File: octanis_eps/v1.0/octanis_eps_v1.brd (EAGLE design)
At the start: 80 x 50 mm, 155 parts, among them IC1 OPA2333DGK, Q1 32.768kHz, Q100 BSS123, Q2 BSC0901NS, U1 CSD16327Q3_DQG_8, U10 CSD16327Q3_DQG_8, U11 CSD16327Q3_DQG_8, U12 TPS630250YFFT, U15 MSP430FR5969, U2 CSD16327Q3_DQG_8, U3 CSD16327Q3_DQG_8, U5 TPS2022D, U6 TPS630250YFFT, U7 TPS630250YFFT, U8 TPS61232, U9 BQ24650_RVA_16

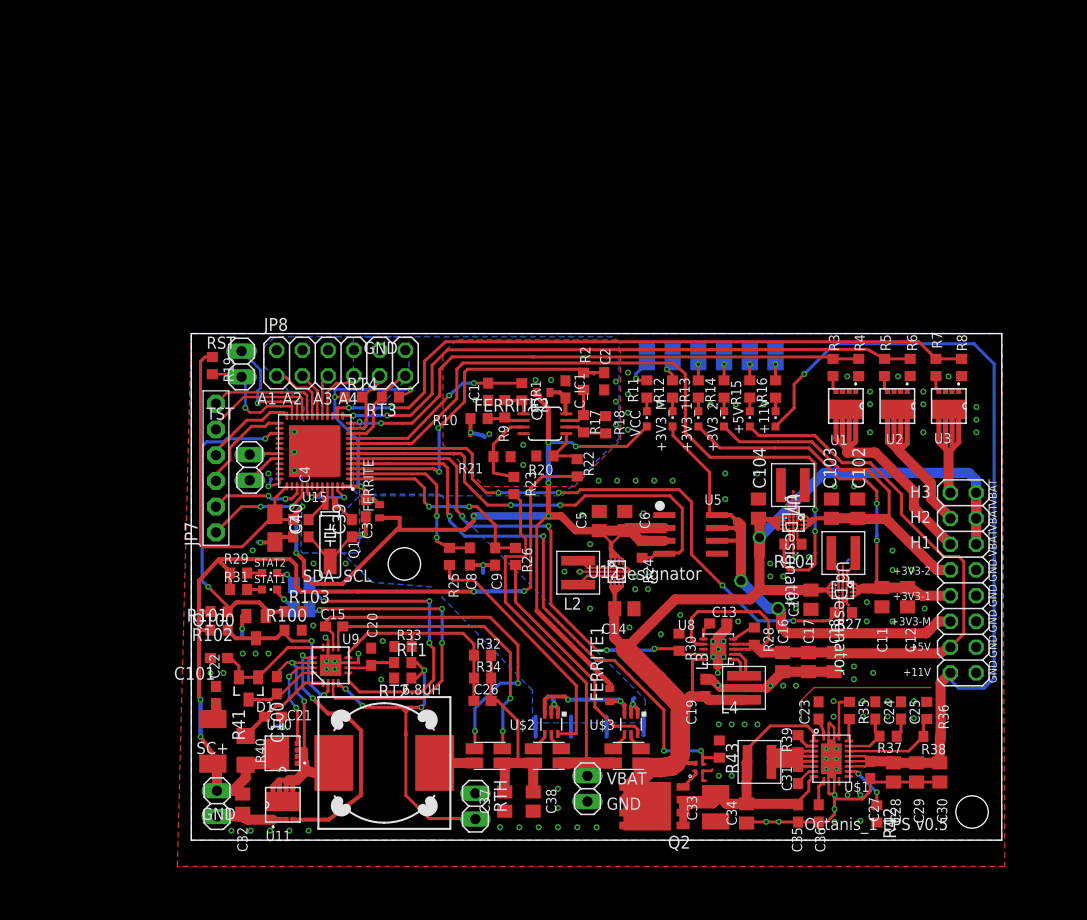
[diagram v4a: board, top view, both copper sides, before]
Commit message: removed ground loops
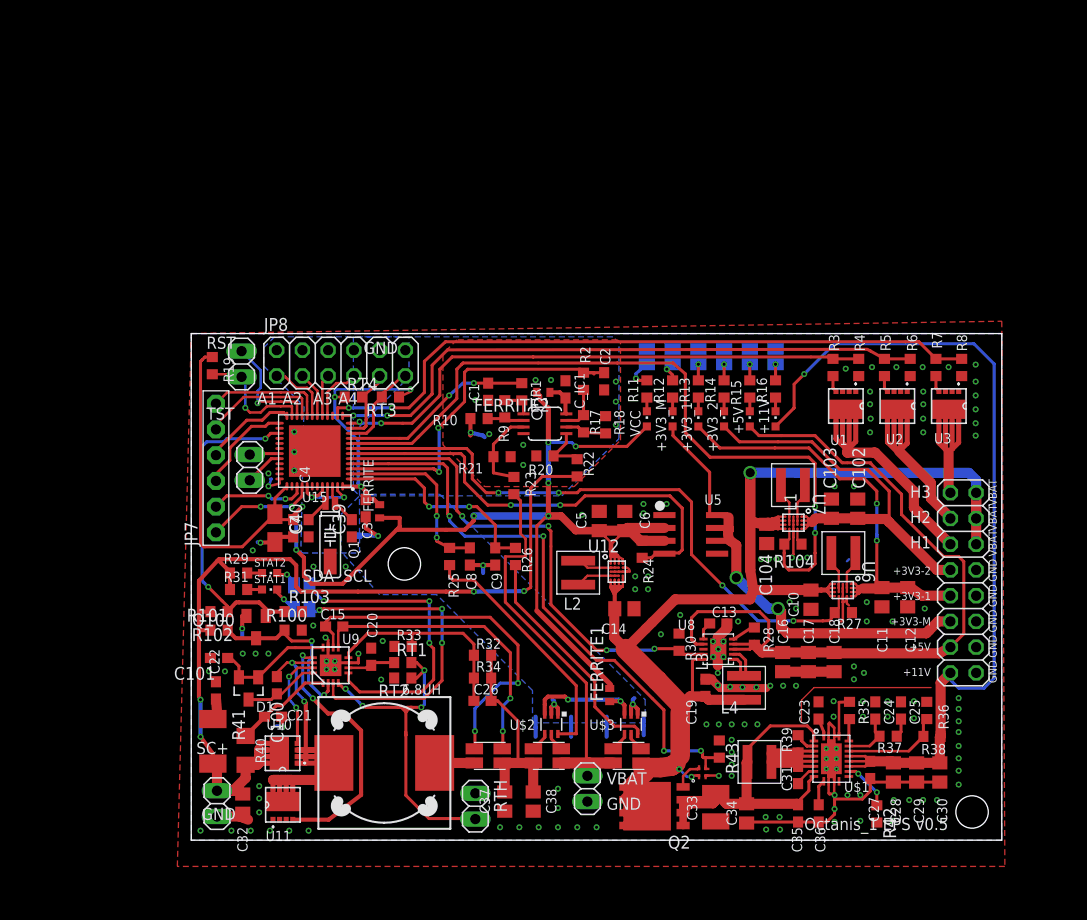
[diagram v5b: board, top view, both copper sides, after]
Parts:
- removed U$4: MIC4414, Octanis1_EPS:QFN-4
- added U$5: MIC5019, Octanis1_EPS:QFN-4
- moved C104 2.62 mm to (56.8, 30.2), turned to 270 degrees
- moved C22 0.46 mm to (2.44, 14.8)
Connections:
- net AGND: no longer C39.1, C40.1, Q1.P3
- net BAT_OUT: now also U$5.P$1, U$5.P1; no longer U$4.P$4, U$4.P4
- net EN_12V: now also U$5.P$3, U$5.P3; no longer U$4.P$3, U$4.P3
- net GND: now also C39.1, C40.1, Q1.P3, U$5.P$2, U$5.P2; no longer U$4.P$2, U$4.P2
- net N$10: now also U$5.P$4, U$5.P4; no longer U$4.P$1, U$4.P1
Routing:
- net N$76: track 29.8 -> 48.1 mm
- net GND: track 122.7 -> 106.9 mm, vias 123 -> 134
- net BAT_OUT: track 131.9 -> 146.9 mm, vias 1 -> 3
- net AGND: track 36.5 -> 30.6 mm
- net SC+: track 88.6 -> 92.3 mm
- net +3V3_M: track 49.7 -> 46.9 mm
- net +3V3_2: track 43.5 -> 42.5 mm
- net N$10: track 2.16 -> 2.99 mm

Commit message: reworked silkscreen
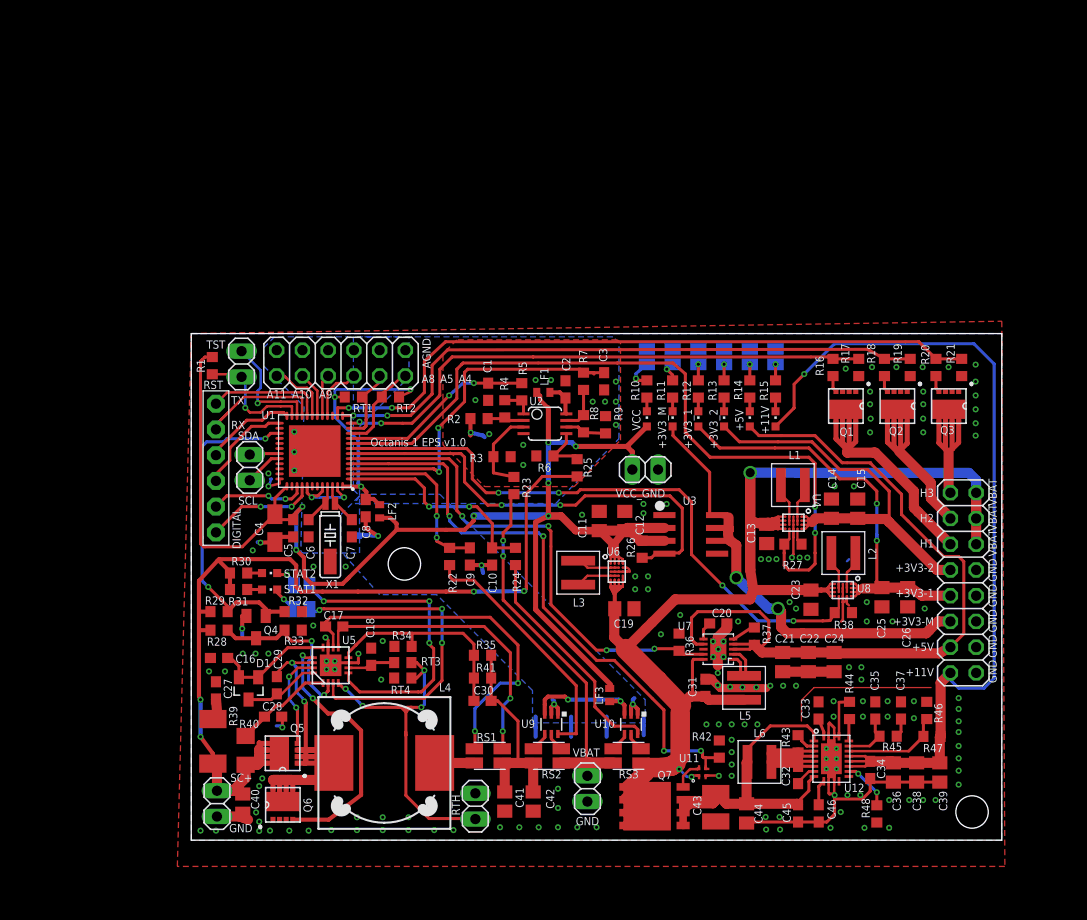
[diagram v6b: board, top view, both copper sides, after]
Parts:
- removed 6.8UH: DR127, inductors:DR127
- removed C100, C_IC1: 100nF, rcl:C0603
- removed C101: 1uF, rcl:C0603
- removed C102, C103: 22uF, resistor:C0805
- removed C104: 10uF, resistor:C0805
- removed IC1: OPA2333DGK, linear:MSOP08
- removed JP8: (no value), Headerlibrary:2X06
- removed L100: 1uH, Coilcraft:XFL4020
- removed R100, R101: (no value), rcl:R0603
- removed R102, R103: 1M, rcl:R0603
- removed R104: 1M, resistor:R0603
- removed U$1: TPS61088, texasinstruments:R-PVQFN-N20
- removed U$2, U$3: INA213, Octanis1_EPS:SC70-6
- removed U$5: MIC5019, Octanis1_EPS:QFN-4
- removed U15: MSP430FR5969, chips:S-PVQFN-N48
- added C41, C42, C44: 10uF, resistor:C0805
- added C43: 47uF Tantal, rcl:C1210
- added C45: 100nF, rcl:C0603
- added C46: 47nF, rcl:C0603
- added JP1, VCC_GND: (no value), Headerlibrary:1X02
- added L5: 1uH, Coilcraft:XFL4020
- added L6: 1.5uH, Coilcraft:XFL4020
- added Q3, Q5, Q6: CSD16327Q3_DQG_8, texasinstruments:DQG8
- added Q7: BSC0901NS, transistor-power:PG-TDSON-8
- added R44: 100k, resistor:R0603
- added R45: 150-220k, resistor:R0603
- added R46: 56k, resistor:R0603
- added R47: 470k, resistor:R0603
- added R48: dnp, resistor:R0603
- added U4: TPS630250YFFT, texasinstruments:YFF0020AEBA
- added X1: 32.768kHz, microcrystal:MS3V-T1R
- C10: value 10uF -> 1.5uF; device resistor:C0805 -> rcl:C0603
- C13: value 10nF -> 10uF; device rcl:C0603 -> resistor:C0805
- C14, C38: value 10uF -> 22uF
- C15: value 100nF -> 22uF; device rcl:C0603 -> resistor:C0805
- C16, C18: value 22uF -> 1uF; device resistor:C0805 -> rcl:C0603
- C17, C29, C5: value 22uF -> 100nF; device resistor:C0805 -> rcl:C0603
- C19: value 22uF -> 10uF; device rcl:C0603 -> resistor:C0805
- C2, C8: value 1.5uF -> 100nF
- C20: value 1uF -> 10nF
- C21: value 1u -> 22uF; device rcl:C0603 -> resistor:C0805
- C22: value 2.2uF -> 22uF; device rcl:C0603 -> resistor:C0805
- C23: value 2.2uF -> 10uF; device rcl:C0603 -> resistor:C0805
- C24: value 150pF -> 22uF; device rcl:C0603 -> resistor:C0805
- C25: value 4.7nF -> 22uF; device rcl:C0603 -> resistor:C0805
- C26: value 22pF -> 22uF; device rcl:C0603 -> resistor:C0805
- C27: value 1uF -> 2.2uF
- C28: value 22uF -> 1u; device resistor:C0805 -> rcl:C0603
- C3: value 100nF -> 1.5uF
- C30: value 22uF -> 22pF; device resistor:C0805 -> rcl:C0603
- C31: value 100nF -> 22uF
- C32: value 10uF -> 100nF; device resistor:C0805 -> rcl:C0603
- C33: value 47uF Tantal -> 2.2uF; device rcl:C1210 -> rcl:C0603
- C34: value 10uF -> 1uF; device resistor:C0805 -> rcl:C0603
- C35: value 100nF -> 150pF
- C36: value 47nF -> 22uF; device rcl:C0603 -> resistor:C0805
- C37: value 10uF -> 4.7nF; device resistor:C0805 -> rcl:C0603
- C39: value 12pF -> 22uF; device rcl:C0603 -> resistor:C0805
- C4: value 100nF -> 10uF; device rcl:C0603 -> rcl:A/3216-18R
- C40: value 12pF -> 10uF; device rcl:C0603 -> resistor:C0805
- C6: value 22uF -> 12pF; device resistor:C0805 -> rcl:C0603
- C7: value 10uF -> 12pF; device rcl:A/3216-18R -> rcl:C0603
- JP2: device Headerlibrary:1X02 -> Headerlibrary:2X06
- L4: value 1.5uH -> DR127_6u8; device Coilcraft:XFL4020 -> inductors:DR127
- Q1: value 32.768kHz -> CSD16327Q3_DQG_8; device microcrystal:MS3V-T1R -> texasinstruments:DQG8
- Q2: value BSC0901NS -> CSD16327Q3_DQG_8; device transistor-power:PG-TDSON-8 -> texasinstruments:DQG8
- R1: value 1k -> 10k
- R10, R18, R22: value 200k -> 1k
- R14: value 1k -> 1.5k
- R15: value 1.5k -> 4.7k
- R16: value 4.7k -> 1k
- R17, R21, R32: value 100k -> 1M
- R19: value 10k -> 1M
- R2, R25: value 1k -> 200k
- R20: value 100k -> 1k
- R24: value 1M -> 1k; device resistor:R0603 -> rcl:R0603
- R26: value 1k -> 1M; device rcl:R0603 -> resistor:R0603
- R29: value 4k7 -> (none)
- R3: value 1k -> 100k
- R30: value 1M -> 4k7
- R33: value 100k -> (none)
- R34: value 2.2M -> 100k
- R35: device resistor:R0603 -> rcl:R0603
- R36: value 56k -> 1M; device resistor:R0603 -> rcl:R0603
- R37: value 150-220k -> 1M; device resistor:R0603 -> rcl:R0603
- R38: value 470k -> 1M
- R39: value 47k -> 2; device resistor:R0603 -> rcl:R2010
- R4, R6, R8: value 1M -> 100k
- R41: value 2 -> 2.2M; device rcl:R2010 -> rcl:R0603
- R42: value dnp -> 1M; device resistor:R0603 -> rcl:R0603
- R43: value 1M -> 47k; device rcl:R0603 -> resistor:R0603
- R9: value 100k -> 200k
- RS1: value RSENSE1 10mOhm -> 10m
- RS2: value RSENSE2 -> 50m
- RS3: value RSENSE1 -> 50m
- RT2: value 8501 -> 2723
- RT4: value 2723 -> 8501
- U1: value CSD16327Q3_DQG_8 -> MSP430FR5969; device texasinstruments:DQG8 -> chips:S-PVQFN-N48
- U10: value CSD16327Q3_DQG_8 -> INA213; device texasinstruments:DQG8 -> Octanis1_EPS:SC70-6
- U11: value CSD16327Q3_DQG_8 -> MIC5019; device texasinstruments:DQG8 -> Octanis1_EPS:QFN-4
- U12: value TPS630250YFFT -> TPS61088; device texasinstruments:YFF0020AEBA -> texasinstruments:R-PVQFN-N20
- U2: value CSD16327Q3_DQG_8 -> OPA2333DGK; device texasinstruments:DQG8 -> linear:MSOP08
- U3: value CSD16327Q3_DQG_8 -> TPS2022D; device texasinstruments:DQG8 -> Octanis1_EPS:SO8
- U5: value TPS2022D -> BQ24650_RVA_16; device Octanis1_EPS:SO8 -> octanis_eps_v05:RVA16_2P14X2P14
- U7: value TPS630250YFFT -> TPS61232; device texasinstruments:YFF0020AEBA -> texasinstruments:S-PVSON-N10
- U8: value TPS61232 -> TPS630250YFFT; device texasinstruments:S-PVSON-N10 -> texasinstruments:YFF0020AEBA
- U9: value BQ24650_RVA_16 -> INA213; device octanis_eps_v05:RVA16_2P14X2P14 -> Octanis1_EPS:SC70-6
- moved R19 68.9 mm to (71.0, 46.7), turned to 270 degrees
- moved C27 65.1 mm to (2.44, 14.8)
- moved C29 63.7 mm to (8.45, 15.3), turned to 270 degrees
- moved C39 62.8 mm to (73.9, 6.68)
- moved C28 61.5 mm to (8.08, 12.2), turned to 0 degrees
- moved C22 58.5 mm to (60.9, 17.6), turned to 270 degrees
- moved R39 57.8 mm to (2.13, 9.75)
- moved C16 55.6 mm to (2.74, 18.0), turned to 180 degrees
- moved C32 54.9 mm to (59.9, 6.43), turned to 270 degrees
- moved C15 53.0 mm to (65.8, 32.7), turned to 90 degrees
- moved R28 52.9 mm to (2.74, 22.6), turned to 180 degrees
- moved Q1 52.8 mm to (64.6, 42.8), turned to 270 degrees
- moved U1 52.6 mm to (12.2, 38.4), turned to 180 degrees
- moved C21 50.6 mm to (58.4, 17.6), turned to 270 degrees
- moved C17 46.9 mm to (14.1, 21.1), turned to 180 degrees
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- renumbered FERRITE to LF2, FERRITE1 to LF3, FERRITE2 to LF1, J1 to J107, J2 to J106, J3 to J105, J4 to J104, J5 to J103, J6 to J102, J7 to J101, J8 to J100, JP7 to DIGITAL, Q100 to Q4, RSENSE1 to RS2, R_SENSE1 to RS1, R_SENSE2 to RS3
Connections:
- net +12V: now also C34.2, C36.2, C38.2, C39.2, R47.2, U12.P$14, U12.P$15, U12.P$16; no longer C27.2, C28.2, C29.2, C30.2, R38.2, U$1.P$14, U$1.P$15, U$1.P$16
- net +3V3: now also C11.1, C12.1, C4.+, R1.2, R26.2, U1.37, U3.2, U3.3, U6.1, U6.2, U6.3, U6.4, VCC_GND.1; no longer C4.1, C6.1, C7.+, R19.2, R24.2, U12.1, U12.2, U12.3, U12.4, U15.37, U5.2, U5.3
- net +3V3_1: now also C25.1, C26.1, U8.1, U8.2, U8.3, U8.4; no longer C11.1, C12.1, U6.1, U6.2, U6.3, U6.4
- net +3V3_2: now also C14.1, C15.1, U4.1, U4.2, U4.3, U4.4; no longer C102.1, C103.1, U7.1, U7.2, U7.3, U7.4
- net +3V3_M: now also U3.6, U3.7, U3.8; no longer U5.6, U5.7, U5.8
- net +5V: now also C21.1, C22.1, C24.1, R37.2, U7.3, U7.4, U7.7; no longer C16.1, C17.1, C18.1, R28.2, U8.3, U8.4, U8.7
- net A4_EXT: now also JP2.11, RT2.2, U1.10; no longer JP8.11, RT3.2, U15.10
- net A5_EXT: now also JP2.9, RT1.2, U1.11; no longer JP8.9, RT4.2, U15.11
- net AGND: now also C10.1, C3.1, C8.2, JP2.10, JP2.12, JP2.2, JP2.4, JP2.6, JP2.8, R2.2, R3.1, R6.1, R9.2, U1.41, U1.44, U1.47, U10.1, U10.2, U2.4, U9.1, U9.2; no longer C3.2, C8.1, C_IC1.1, IC1.4, JP8.10, JP8.12, JP8.2, JP8.4, JP8.6, JP8.8, R10.2, R18.2, R20.1, R21.1, U$2.1, U$2.2, U$3.1, U$3.2, U15.41, U15.44, U15.47
- net AVCC: now also C8.1, RT1.1, RT2.1, U1.48; no longer C3.1, RT3.1, RT4.1, U15.48
- net AVCC1: now also U10.3, U9.3; no longer U$2.3, U$3.3
- net AVCC2: now also C2.2, U2.8; no longer C_IC1.2, IC1.8
- net A_EXT1: now also JP2.7, U1.16; no longer JP8.7, U15.16
- net A_EXT2: now also JP2.5, U1.17; no longer JP8.5, U15.17
- net A_EXT3: now also JP2.3, U1.18; no longer JP8.3, U15.18
- net A_EXT4: now also JP2.1, U1.19; no longer JP8.1, U15.19
- net BAT_11V: now also C43.1, C44.1, C45.1, L6.P$1, Q7.1, Q7.2, Q7.3, U12.P$2, U12.P$9; no longer C33.1, C34.1, C35.1, L4.P$1, Q2.1, Q2.2, Q2.3, U$1.P$2, U$1.P$9
- net BAT_OUT: now also C13.1, C23.1, C31.1, L5.P$1, Q7.5, Q7.6, Q7.7, Q7.8, U11.P$1, U11.P1, U4.17, U4.18, U4.19, U4.20, U6.16, U7.10, U8.17, U8.18, U8.19, U8.20; no longer C10.1, C104.1, C14.1, L3.P$1, Q2.5, Q2.6, Q2.7, Q2.8, U$5.P$1, U$5.P1, U12.16, U12.17, U12.18, U12.19, U12.20, U7.17, U7.18, U7.19, U7.20, U8.10
- net EN_12V: now also R42.2, U1.4, U11.P$3, U11.P3; no longer R43.2, U$5.P$3, U$5.P3, U15.4
- net EN_3V3_1: now also R38.1, U1.7, U8.16; no longer R27.1, U15.7, U6.16
- net EN_3V3_2: now also R27.1, U1.8, U4.16; no longer R104.1, U15.8, U7.16
- net EN_3V3_M: now also R26.1, U1.6, U3.4; no longer R24.1, U15.6, U5.4
- net EN_5V: now also R36.2, U1.5, U7.9; no longer R30.2, U15.5, U8.9
- net EN_HEAT1: now also R16.2, R17.1, U1.12; no longer R3.2, R4.1, U15.12
- net EN_HEAT2: now also R18.2, R19.1, U1.13; no longer R5.2, R6.1, U15.13
- net EN_HEAT3: now also R20.2, R21.1, U1.14; no longer R7.2, R8.1, U15.14
- net EN_SC: now also R28.1, R32.2, U1.27; no longer R102.1, R103.2, U15.27
- net GND: now also C15.2, C26.2, C27.2, C28.2, C31.2, C34.1, C36.1, C38.1, C4.-, C41.2, C42.2, C43.2, C44.2, C45.2, C46.2, C6.1, C7.1, Q1.1, Q1.2, Q1.3, Q2.1, Q2.2, Q2.3, Q3.1, Q3.2, Q3.3, Q6.1, Q6.2, Q6.3, R17.2, R19.2, R21.2, R32.1, R34.1, R38.2, R42.1, R44.1, R46.1, R48.2, RT4.2, U1.36, U1.VSS_QFN, U11.P$2, U11.P2, U12.P$20, U12.PGND1, U12.PGND10, U12.PGND11, U12.PGND12, U12.PGND2, U12.PGND3, U12.PGND4, U12.PGND5, U12.PGND6, U12.PGND7, U12.PGND8, U12.PGND9, U4.10, U4.11, U4.12, U4.8, U4.9, U5.11, U5.17, U5.7, U5.V, U5.V_1, U5.V_2, U5.V_3, U7.EXPAD, U7.GND1, U7.GND2, U7.GND3, U7.GND4, U7.GND5, U8.10, U8.11, U8.12, U8.8, U8.9, VCC_GND.2, X1.P3; no longer C10.2, C101.2, C102.2, C103.2, C104.2, C17.2, C27.1, C28.1, C29.1, C30.1, C32.1, C34.2, C36.2, C38.2, C4.2, C6.2, C7.-, Q1.P3, R100.1, R103.1, R104.2, R30.1, R35.1, R4.2, R42.2, R43.1, R6.2, R8.2, RT2.2, U$1.P$20, U$1.PGND1, U$1.PGND10, U$1.PGND11, U$1.PGND12, U$1.PGND2, U$1.PGND3, U$1.PGND4, U$1.PGND5, U$1.PGND6, U$1.PGND7, U$1.PGND8, U$1.PGND9, U$5.P$2, U$5.P2, U1.1, U1.2, U1.3, U11.1, U11.2, U11.3, U12.10, U12.11, U12.12, U12.8, U12.9, U15.36, U15.VSS_QFN, U2.1, U2.2, U2.3, U3.2, U3.3, U5.1, U7.10, U7.11, U7.12, U7.8, U7.9, U8.EXPAD, U8.GND1, U8.GND2, U8.GND3, U8.GND4, U8.GND5, U9.11, U9.17, U9.7, U9.V, U9.V_1, U9.V_2, U9.V_3
- net HEAT1: now also Q1.5, Q1.6, Q1.7, Q1.8; no longer U1.5, U1.6, U1.7, U1.8
- net HEAT2: now also Q2.5, Q2.6, Q2.7, Q2.8; no longer U2.5, U2.6, U2.7, U2.8
- net HEAT3: now also Q3.5, Q3.6, Q3.7, Q3.8; no longer U3.5, U3.6, U3.7, U3.8
- net I2C_SCL: now also U1.32; no longer U15.32
- net I2C_SDA: now also U1.31; no longer U15.31
- net IND: now also L5.P$2, U7.1, U7.2; no longer L3.P$2, U8.1, U8.2
- net I_IN: now also C9.2, R22.1, U1.2; no longer C8.2, R25.1, U15.2
- net I_OUT: now also C10.2, R24.1, U1.1; no longer C9.2, R26.1, U15.1
- net LED5: now also R14.2; no longer R15.2
- net N$1: now also L3.P$1, U6.13, U6.14, U6.15; no longer L2.P$1, U12.13, U12.14, U12.15
- net N$10: now also Q7.4, U11.P$4, U11.P4; no longer Q2.4, U$5.P$4, U$5.P4
- net N$11: now also L1.P$1, U4.13, U4.14, U4.15; no longer L100.P$1, U7.13, U7.14, U7.15
- net N$12: now also L1.P$2, U4.5, U4.6, U4.7; no longer L100.P$2, U7.5, U7.6, U7.7
- net N$13: now also JP1.1, R1.1, U1.23; no longer JP2.1, R19.1, U15.23
- net N$14: now also R14.1; no longer R15.1
- net N$15: now also JP1.2, U1.22; no longer JP2.2, U15.22
- net N$16: now also C7.2, U1.46, X1.P1; no longer C39.2, Q1.P1, U15.46
- net N$17: now also C6.2, U1.45, X1.P2; no longer C40.2, Q1.P2, U15.45
- net N$18: now also U1.25; no longer U15.25
- net N$19: now also R4.1, R5.2, U2.1; no longer IC1.1, R1.2, R9.1
- net N$2: now also R37.1, U7.5; no longer R28.1, U8.5
- net N$20: now also R2.1, R4.2, U2.2; no longer IC1.2, R10.1, R9.2
- net N$21: now also R3.2, U2.3; no longer IC1.3, R21.2
- net N$22: now also R7.2, R8.1, U2.7; no longer IC1.7, R17.1, R2.2
- net N$23: now also R8.2, R9.1, U2.6; no longer IC1.6, R17.2, R18.1
- net N$24: now also R25.1, R6.2, U2.5; no longer IC1.5, R20.2, R22.1
- net N$25: now also R24.2, U10.6; no longer R26.2, U$3.6
- net N$26: now also R22.2, U9.6; no longer R25.2, U$2.6
- net N$27: now also Q3.4, R20.1; no longer R7.1, U3.4
- net N$28: now also U1.24; no longer U15.24
- net N$29: now also U1.39; no longer U15.39
- net N$3: now also L3.P$2, U6.5, U6.6, U6.7; no longer L2.P$2, U12.5, U12.6, U12.7
- net N$30: now also U1.40; no longer U15.40
- net N$31: now also Q2.4, R18.1; no longer R5.1, U2.4
- net N$32: now also U10.4; no longer U$3.4
- net N$33: now also U10.5; no longer U$3.5
- net N$34: now also U9.4; no longer U$2.4
- net N$35: now also U9.5; no longer U$2.5
- net N$36: now also U1.21; no longer U15.21
- net N$37: now also Q1.4, R16.1; no longer R3.1, U1.4
- net N$38: now also C32.2, U12.P$8; no longer C31.2, U$1.P$8
- net N$39: now also R11.2; no longer R12.2
- net N$4: now also L4.2; no longer 6.8UH.2
- net N$40: now also R11.1; no longer R12.1
- net N$41: now also U1.20; no longer U15.20
- net N$42: now also C27.1, R39.1; no longer C22.1, R41.1
- net N$43: now also R10.2; no longer R11.2
- net N$45: now also R10.1; no longer R11.1
- net N$46: now also R13.2; no longer R14.2
- net N$47: now also R13.1; no longer R14.1
- net N$48: now also R15.2; no longer R16.2
- net N$49: now also R15.1; no longer R16.1
- net N$5: now also C20.1, U7.6; no longer C13.1, U8.6
- net N$50: now also C32.1, L6.P$2, R43.2, U12.P$4, U12.P$5, U12.P$6, U12.P$7; no longer C31.1, L4.P$2, R39.2, U$1.P$4, U$1.P$5, U$1.P$6, U$1.P$7
- net N$51: now also R12.2; no longer R13.2
- net N$52: now also R12.1; no longer R13.1
- net N$53: now also R43.1, U12.P$3; no longer R39.1, U$1.P$3
- net N$54: now also C37.1, R45.1; no longer C25.1, R37.1
- net N$56: now also C46.1, U12.P$10; no longer C36.1, U$1.P$10
- net N$57: now also R44.2, U12.P$19; no longer R35.2, U$1.P$19
- net N$58: now also C35.1, R45.2, U12.P$18; no longer C24.1, R37.2, U$1.P$18
- net N$59: now also C33.1, U12.P$1; no longer C23.1, U$1.P$1
- net N$6: now also L2.P$1, U8.13, U8.14, U8.15; no longer L1.P$1, U6.13, U6.14, U6.15
- net N$60: now also R46.2, R47.1, U12.P$17; no longer R36.2, R38.1, U$1.P$17
- net N$64: now also R29.1, R33.2, U5.2; no longer R100.2, R101.1, U9.2
- net N$69: now also R30.1; no longer R29.1
- net N$7: now also L2.P$2, U8.5, U8.6, U8.7; no longer L1.P$2, U6.5, U6.6, U6.7
- net N$70: now also U5.5; no longer U9.5
- net N$71: now also U5.3; no longer U9.3
- net N$72: now also C18.1, RT3.1, U5.6; no longer C20.1, RT1.1, U9.6
- net N$73: now also C28.1, U5.1; no longer C21.1, U9.1
- net N$76: now also C29.1, L4.1, Q5.1, Q5.2, Q5.3, Q6.5, Q6.6, Q6.7, Q6.8, U5.14; no longer 6.8UH.1, C100.1, U10.1, U10.2, U10.3, U11.5, U11.6, U11.7, U11.8, U9.14
- net N$77: now also C17.2, U5.10; no longer C15.2, U9.10
- net N$78: now also C17.1, U5.9; no longer C15.1, U9.9
- net N$80: now also Q5.4, U5.15; no longer U10.4, U9.15
- net N$81: now also Q6.4, U5.13; no longer U11.4, U9.13
- net N$82: now also C30.2, R34.2, R35.1, R41.1, U5.8; no longer C26.2, R32.1, R33.2, R34.1, U9.8
- net N$84: now also C16.1, U5.12; no longer C101.1, U9.12
- net N$85: now also C29.2, U5.16; no longer C100.2, U9.16
- net N$9: now also R48.1, U12.P$13; no longer R42.1, U$1.P$13
- net SC+: now also C40.2, Q5.5, Q5.6, Q5.7, Q5.8, R25.2, R28.2, R30.2, R39.2; no longer C32.2, R101.2, R102.2, R22.2, R41.2, U10.5, U10.6, U10.7, U10.8
- net SC_OUT: now also C30.1, C41.1, C42.1, R35.2, R41.2; no longer C26.1, C37.1, C38.1, R32.2, R34.2
- net TS: now also RT3.2, RT4.1, U5.4; no longer RT1.2, RT2.1, U9.4
- net V_BAT: now also R5.1, U1.9; no longer R1.1, U15.9
- net V_SC: now also C3.2, R7.1, U1.3; no longer C2.2, R2.1, U15.3
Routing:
- net +3V3: track 148.0 -> 150.6 mm
- net BAT+: track 41.2 -> 39.2 mm, vias 0 -> 2
- net N$36: track 11.9 -> 13.8 mm
- net AGND: vias 16 -> 18
- net GND: vias 134 -> 144
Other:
- board text added: "A10"
- board text added: "A11"
- board text added: "A5"
- board text added: "A8"
- board text added: "A9"
- board text added: "AGND"
- board text added: "Electrical Power Subsystem"
- board text added: "L5"
- board text added: "L6"
- board text added: "Octanis 1 EPS v1.0"
- board text added: "RS1"
- board text added: "RS2"
- board text added: "RS3"
- board text added: "RX"
- board text added: "TX"
- board text added: "www.octanis.org"
- board text removed: "A1"
- board text removed: "A2"
- board text removed: "A3"
- board text removed: "L100"
- board text removed: "L4"
- board text removed: "Octanis_1 EPS v0.5"

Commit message: final silk and minor copper rework. files ready for production
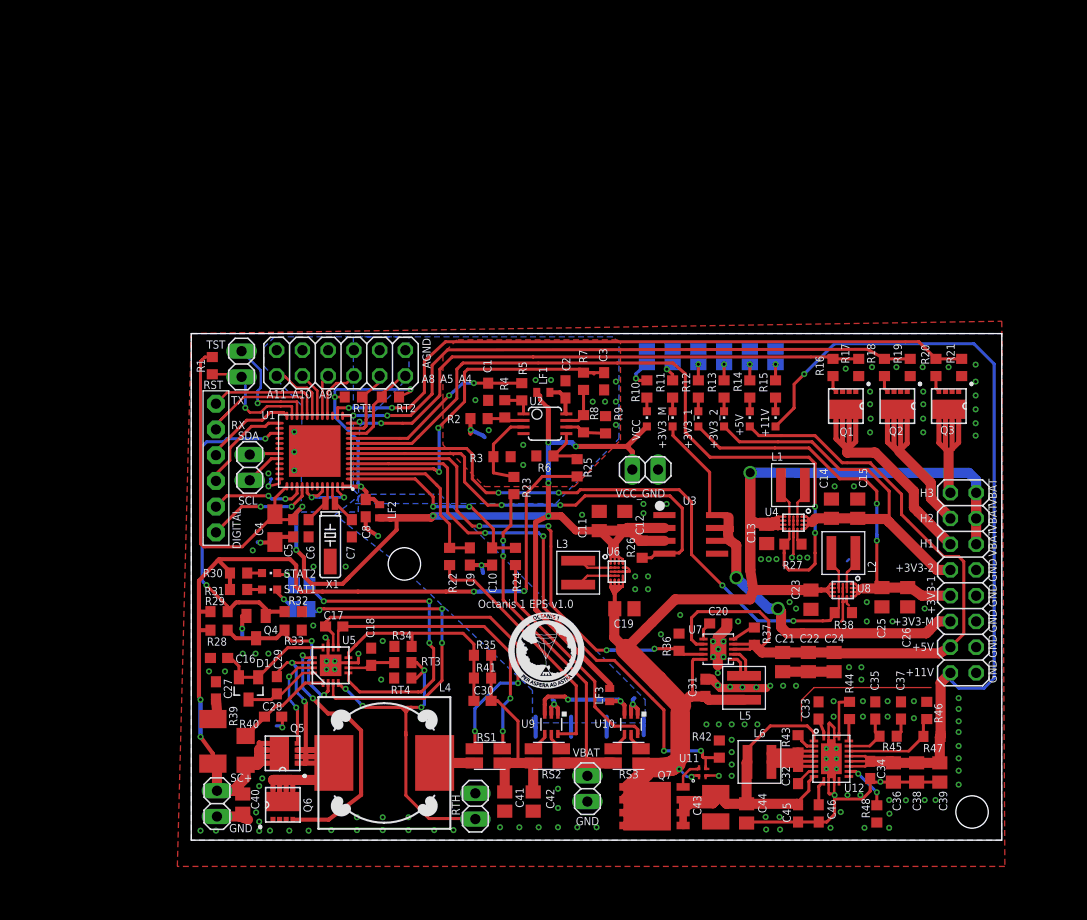
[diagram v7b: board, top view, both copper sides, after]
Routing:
- net AGND: track 30.6 -> 27.3 mm
- net +3V3: track 150.6 -> 151.9 mm
- net GND: track 106.9 -> 105.7 mm, vias 144 -> 146
- net I_IN: track 18.0 -> 17.7 mm, vias 2 -> 0

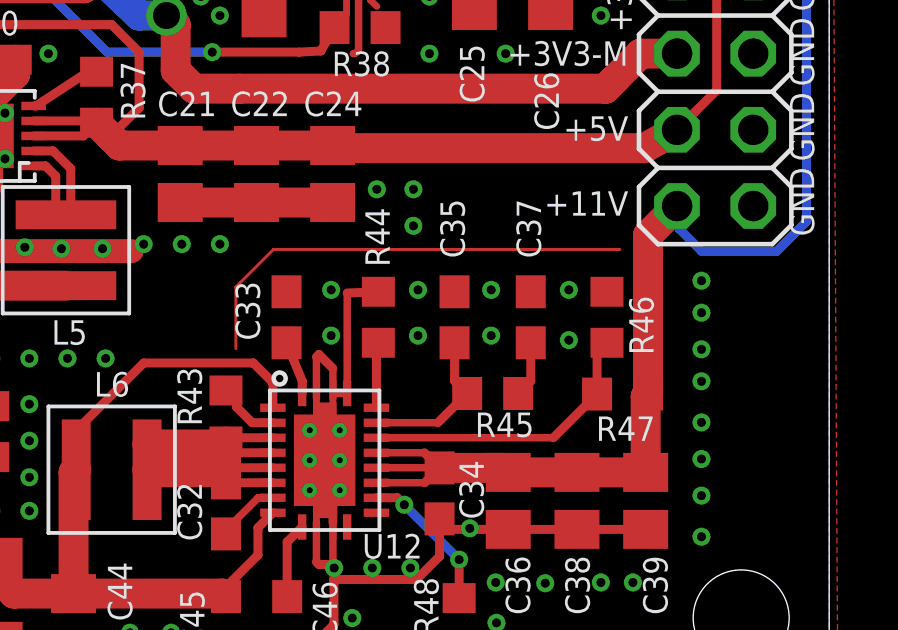
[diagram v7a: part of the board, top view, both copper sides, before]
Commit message: removed stitching at 12V boost; final files that were sent to production
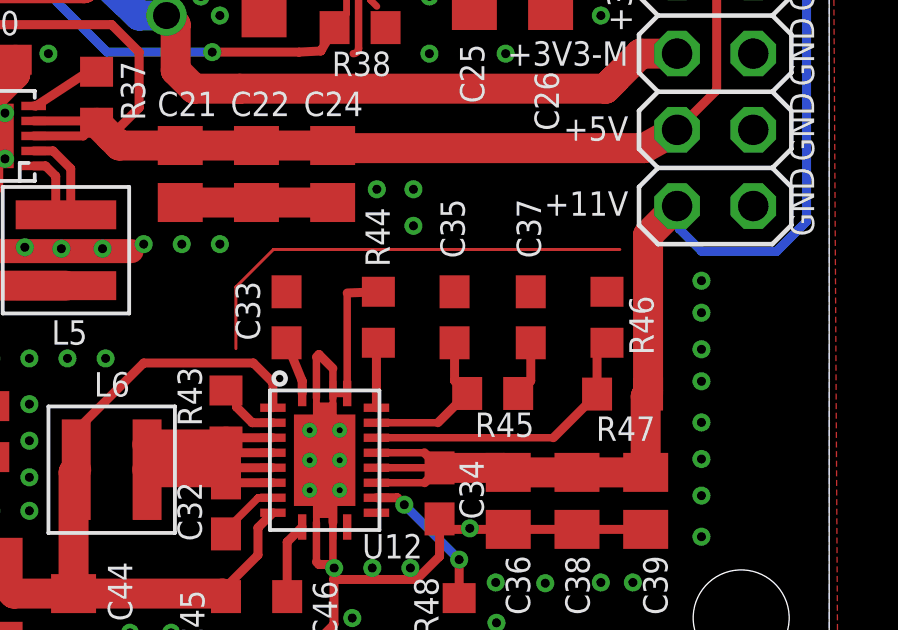
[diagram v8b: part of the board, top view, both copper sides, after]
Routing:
- net GND: vias 146 -> 138
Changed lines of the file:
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@@
 <via x="66.04" y="4.445" extent="1-16" drill="0.3"/>
 <via x="64.77" y="4.445" extent="1-16" drill="0.3"/>
-<via x="63.3984" y="12.192" extent="1-16" drill="0.3"/>
-<via x="63.3984" y="13.716" extent="1-16" drill="0.3"/>
 <via x="57.15" y="15.24" extent="1-16" drill="0.3"/>
 <via x="66.1416" y="17.0688" extent="1-16" drill="0.3"/>
@@
 <wire x1="64.7128" y1="23.895" x2="64.3128" y2="23.495" width="0.25" layer="1" curve="-90"/>
 <via x="66.675" y="23.495" extent="1-16" drill="0.3"/>
-<via x="66.294" y="13.716" extent="1-16" drill="0.3"/>
-<via x="68.7324" y="13.716" extent="1-16" drill="0.3"/>
-<via x="71.3232" y="13.716" extent="1-16" drill="0.3"/>
-<via x="66.294" y="12.192" extent="1-16" drill="0.3"/>
-<via x="68.7324" y="12.192" extent="1-16" drill="0.3"/>
-<via x="71.3232" y="12.0396" extent="1-16" drill="0.3"/>
 <wire x1="33.9852" y1="11.1252" x2="33.9852" y2="10.2108" width="0.4064" layer="16"/>
 <wire x1="37.4904" y1="11.1252" x2="37.4904" y2="10.2108" width="0.4064" layer="16"/>
@@
 <via x="68.8848" y="3.9624" extent="1-16" drill="0.3"/>
 <via x="68.9102" y="2.6162" extent="1-16" drill="0.3"/>
+<wire x1="63.4582" y1="10.1116" x2="63.4582" y2="9.2616" width="0" layer="19" extent="1-1"/>
 </signal>
 <signal name="IND">
